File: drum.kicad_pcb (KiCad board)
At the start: 4 copper layers, 70 x 70 mm, 112 parts, among them J1001 NE8FAH, J101 CORTEX-DEBUG, J102 JAE_DX07S016JA3, J501 WAGO-2065, J502 WAGO-2065, J601 WAGO-2065, J602 WAGO-2065, J701 Conn_01x01, J702 Conn_01x01, J703 Conn_01x01, J704 Conn_01x01, J801 WAGO-2065, J802 WAGO-2065, J803 WAGO-2065, J901 NE8FAH, Q201 BSC010N04LS, Q202 BSC010N04LS, Q501 BSC010N04LS, Q601 BSC010N04LS, SW101 SW_Push, SW102 SW_Push, U1001 THVD24x2, U101 ATSAMD51J, U102 TPS78433QWDRBRQ1, U201 LM74502-Q1, U301 TPSM33625, U401 BTT6010, U701 TMC2130-LA, U801 74AHC1G125, U901 THVD24x2, Y101 32k768

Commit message: Update
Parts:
- moved INFO101 2.55 mm to (121.0, 117.5)
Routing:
- net GND: vias 100 -> 110
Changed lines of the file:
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@@
 	(footprint "V2_Production:Layer_Numbers"
 		(layer "F.Cu")
-		(at 121.5 115 -90)
+		(at 121 117.5 -90)
 		(property "Reference" "INFO101"
 			(at 0 -2.25 270)
@@
 			(polygon
 				(pts
-					(xy 120.9 116.6) (xy 120.9 113.4) (xy 122.1 113.4) (xy 122.1 116.6)
+					(xy 120.4 119.1) (xy 120.4 115.9) (xy 121.6 115.9) (xy 121.6 119.1)
 				)
 			)
@@
 	)
 	(via
+		(at 121 135)
+		(size 0.45)
+		(drill 0.2)
+		(layers "F.Cu" "B.Cu")
+		(remove_unused_layers yes)
+		(keep_end_layers yes)
+		(free yes)
+		(zone_layer_connections "In1.Cu" "In2.Cu")
+		(net 1)
+	)
+	(via
 		(at 160.75 92.25)
 		(size 0.45)
@@
 	)
 	(via
+		(at 121 115)
+		(size 0.45)
+		(drill 0.2)
+		(layers "F.Cu" "B.Cu")
+		(remove_unused_layers yes)
+		(keep_end_layers yes)
+		(free yes)
+		(zone_layer_connections "In1.Cu" "In2.Cu")
+		(net 1)
+	)
+	(via
+		(at 121 120)
+		(size 0.45)
+		(drill 0.2)
+		(layers "F.Cu" "B.Cu")
+		(remove_unused_layers yes)
+		(keep_end_layers yes)
+		(free yes)
+		(zone_layer_connections "In1.Cu" "In2.Cu")
+		(net 1)
+	)
+	(via
 		(at 154.5 108.75)
 		(size 0.45)
@@
 	)
 	(via
+		(at 189 80)
+		(size 0.45)
+		(drill 0.2)
+		(layers "F.Cu" "B.Cu")
+		(remove_unused_layers yes)
+		(keep_end_layers yes)
+		(free yes)
+		(zone_layer_connections "In1.Cu")
+		(net 1)
+	)
+	(via
+		(at 185 71)
+		(size 0.45)
+		(drill 0.2)
+		(layers "F.Cu" "B.Cu")
+		(remove_unused_layers yes)
+		(keep_end_layers yes)
+		(free yes)
+		(zone_layer_connections "In1.Cu")
+		(net 1)
+	)
+	(via
 		(at 160.5 83.5)
 		(size 0.45)
@@
 	)
 	(via
+		(at 145 71)
+		(size 0.45)
+		(drill 0.2)
+		(layers "F.Cu" "B.Cu")
+		(remove_unused_layers yes)
+		(keep_end_layers yes)
+		(free yes)
+		(zone_layer_connections "In1.Cu" "In2.Cu")
+		(net 1)
+	)
+	(via
 		(at 185.75 115.75)
 		(size 0.45)
@@
 	)
 	(via
+		(at 189 75)
+		(size 0.45)
+		(drill 0.2)
+		(layers "F.Cu" "B.Cu")
+		(remove_unused_layers yes)
+		(keep_end_layers yes)
+		(free yes)
+		(zone_layer_connections "In1.Cu")
+		(net 1)
+	)
+	(via
 		(at 166.5 101)
 		(size 0.45)
@@
 	)
 	(via
+		(at 121 125)
+		(size 0.45)
+		(drill 0.2)
+		(layers "F.Cu" "B.Cu")
+		(remove_unused_layers yes)
+		(keep_end_layers yes)
+		(free yes)
+		(zone_layer_connections "In1.Cu" "In2.Cu")
+		(net 1)
+	)
+	(via
 		(at 141.25 92.25)
 		(size 0.45)
@@
 	)
 	(via
+		(at 165 71)
+		(size 0.45)
+		(drill 0.2)
+		(layers "F.Cu" "B.Cu")
+		(remove_unused_layers yes)
+		(keep_end_layers yes)
+		(free yes)
+		(zone_layer_connections "In1.Cu")
+		(net 1)
+	)
+	(via
 		(at 157 104.75)
 		(size 0.45)
@@
 		(size 0.45)
 		(drill 0.2)
+		(layers "F.Cu" "B.Cu")
+		(remove_unused_layers yes)
+		(keep_end_layers yes)
+		(free yes)
+		(zone_layer_connections "In1.Cu" "In2.Cu")
+		(net 1)
+	)
+	(via
+		(at 121 130)
+		(size 0.45)
+		(drill 0.2)

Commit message: Update parts
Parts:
- C1001, C101, C102, C103, C104, C105, C106, C107, C108, C201, C202, C302, C305, C401, C402, C403, C404, C501, C601, C701, C706, C708, C709, C901: footprint Capacitor_SMD:C_0603_1608Metric -> V2_Capacitor_SMD:C_0603
- C109, C110: footprint Capacitor_SMD:C_0805_2012Metric -> V2_Capacitor_SMD:C_0805
- C301, C303, C304, C704, C705: footprint Capacitor_SMD:C_1210_3225Metric -> V2_Capacitor_SMD:C_1210
- C702, C703: footprint Capacitor_SMD:CP_Elec_6.3x5.8 -> V2_Capacitor_SMD:CP_Elec_6.3x7.7
- C707: value 0u470 -> 0u47; footprint Capacitor_SMD:C_0603_1608Metric -> V2_Capacitor_SMD:C_0603
- D101: footprint LED_SMD:LED_0603_1608Metric -> V2_LED:LED_0603
- D401: footprint Diode_SMD:D_SOD-523 -> V2_Diode_SMD:D_SOD-523
- D501, D601: footprint Diode_SMD:D_SOD-123F -> V2_Diode_SMD:D_SOD-123F
- FID101, FID102, FID103: value Fiducial -> Fiducial_Paste
- INFO102: value ORDER-NUMBER -> Order_Number
- J1001, J901: value NE8FAH -> NE8FAV
- J101: value CORTEX-DEBUG -> Cortex_Debug
- J102: value JAE_DX07S016JA3 -> DX07S016JA3
- J501, J502, J601, J602, J801, J802, J803: value WAGO-2065 -> WAGO 2065-100
- J701, J702, J703, J704: value Conn_01x01 -> WAGO 2065-100
- R1001, R101, R102, R103, R104, R201, R202, R301, R302, R401, R402, R403, R404, R405, R406, R407, R408, R409, R410, R701, R901: footprint Resistor_SMD:R_0603_1608Metric -> V2_Resistor_SMD:R_0603
- R702, R703: footprint Resistor_SMD:R_0805_2012Metric -> V2_Resistor_SMD:R_0805
- SW101, SW102: value SW_Push -> SKSG
- TVS101: value SMAJ36CA -> SMBJ36CA; footprint Diode_SMD:D_SMA -> V2_Diode_SMD:D_SMB
- U1001, U901: value THVD24x2 -> THVD2442
- U801: footprint Package_TO_SOT_SMD:SOT-23-5 -> V2_Package_TO_SOT_SMD:SOT-23-5
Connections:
- net USB-Shield renamed Shield

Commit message: Update library
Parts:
- TVS101: value SMBJ36CA -> SMBJ33CA
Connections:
- net +24V renamed +28V
- net /+24V-Supply renamed +VLINK
- net VBUS renamed +VBUS

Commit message: Update library
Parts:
- J101: value Cortex_Debug -> Cortex; footprint V2_Cortex_Debug:Cortex_Debug_Pad -> V2_Connector_Debug:Cortex
- U301: footprint V2_Converter_DCDC:TPSM33625 -> V2_Converter_DCDC:QFN-11
- U701: footprint V2_Driver_Stepper:QFN36-5X6 -> V2_Package_DFN_QFN:QFN36-5X6
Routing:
- net /SWCLK: track 11.3 -> 13.3 mm
- net GND: vias 110 -> 108
- net +3V3: vias 16 -> 15

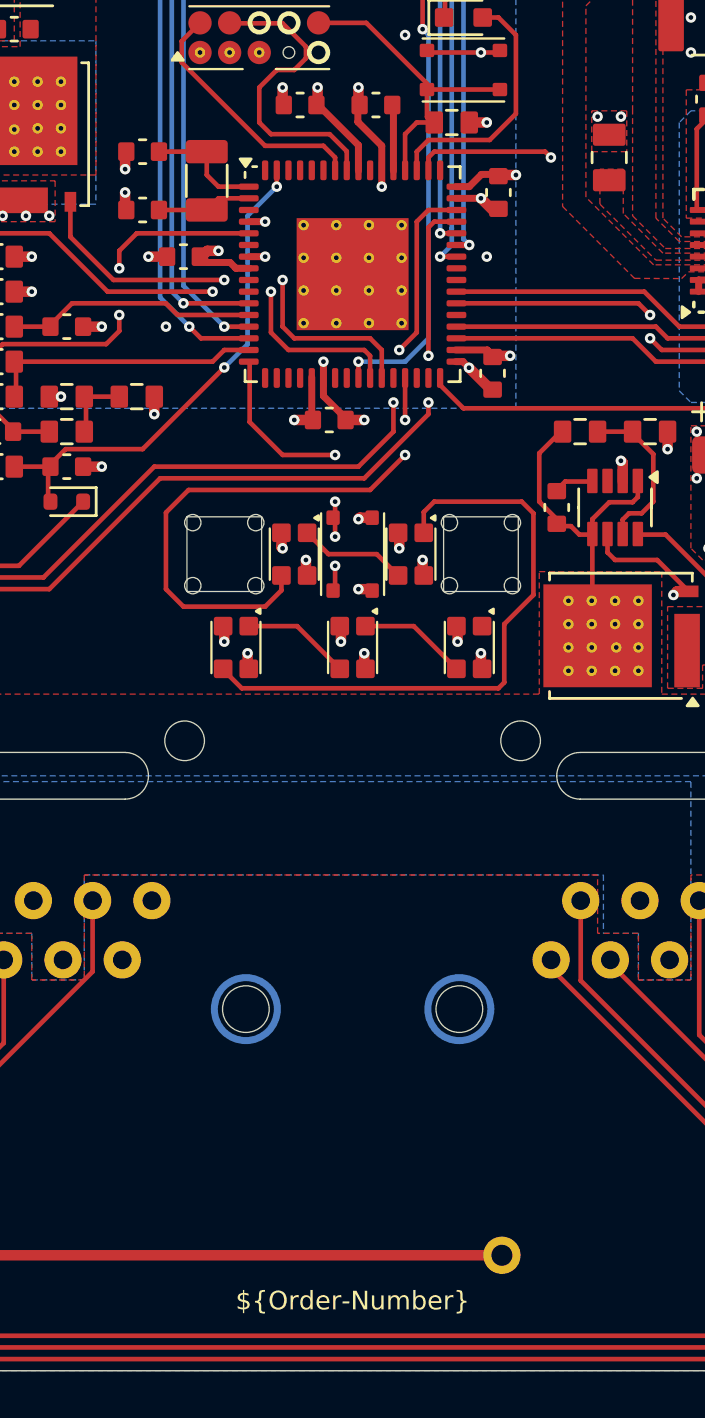
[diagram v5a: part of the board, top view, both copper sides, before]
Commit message: Replace Order_Number
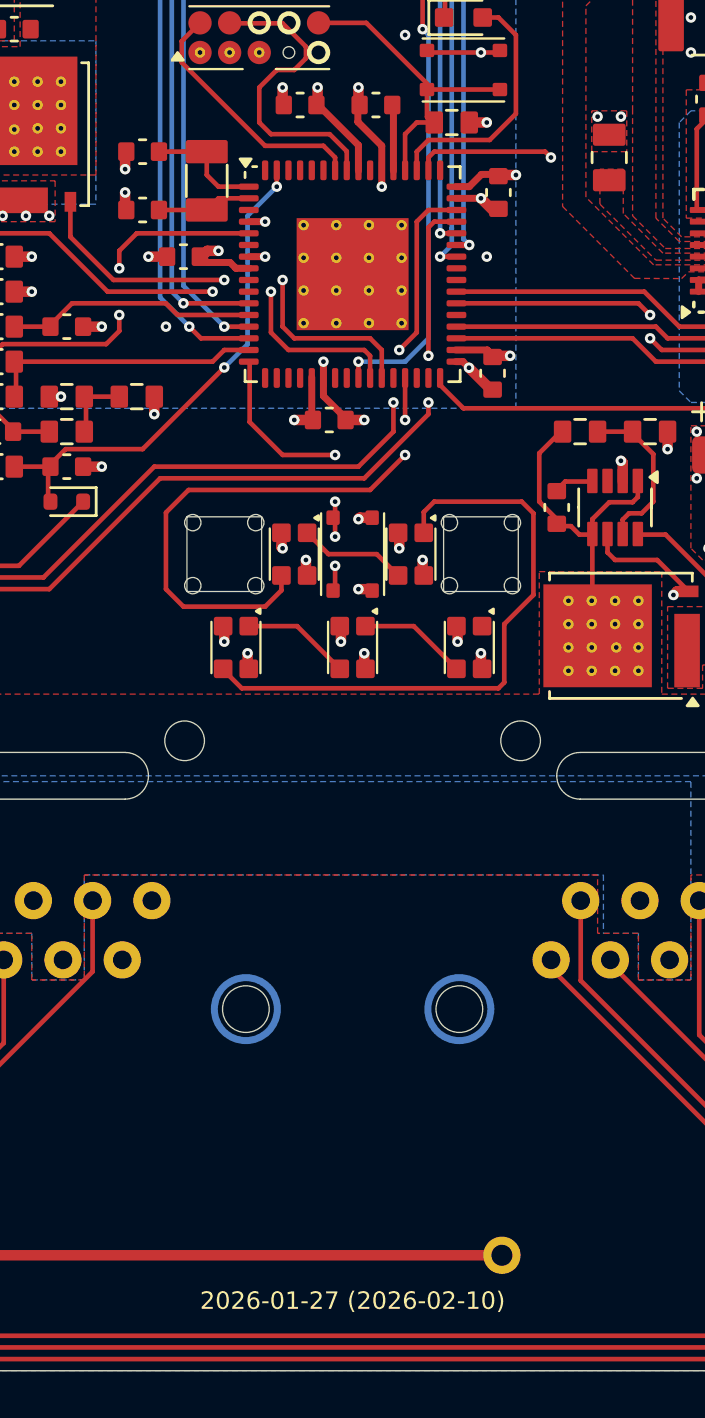
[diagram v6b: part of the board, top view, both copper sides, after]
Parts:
- H101, H102, H103, H104: value MountingHole_3mm -> 3mm
- INFO102: value Order_Number -> ~; footprint V2_Production:Order_Number -> V2_Production:Revision

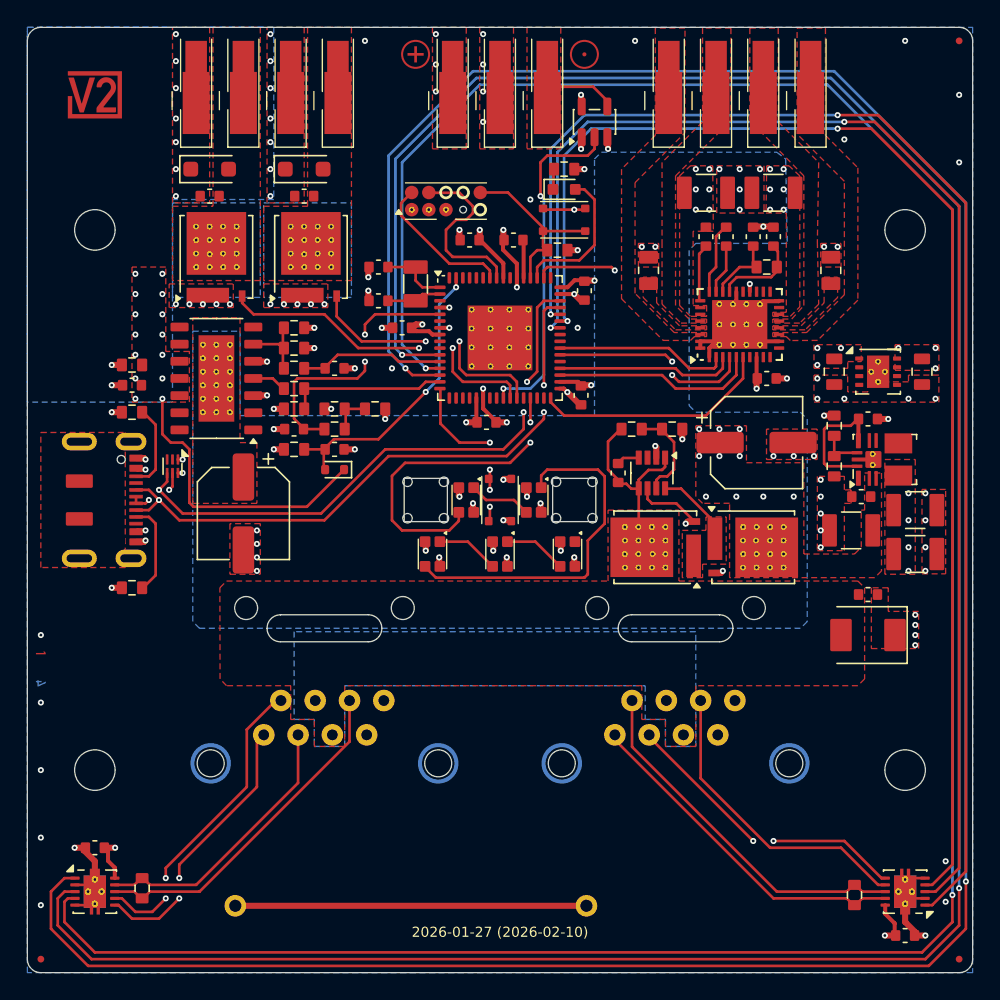
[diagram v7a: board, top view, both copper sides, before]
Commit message: Replace diode
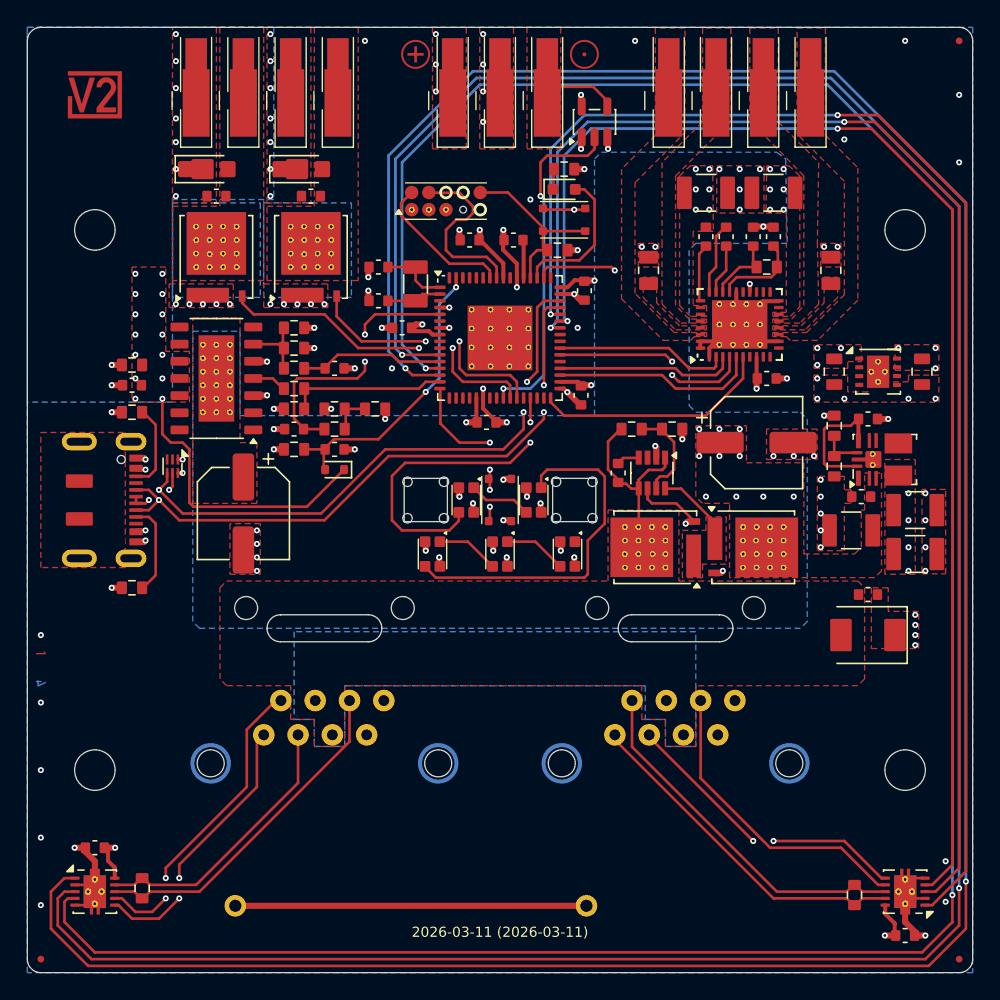
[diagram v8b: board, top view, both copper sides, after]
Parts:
- D501, D601: value S310FA -> PMEG6030AEXEX; footprint V2_Diode_SMD:D_SOD-123F -> V2_Diode_SMD:D_SOD-123HP
- U701: footprint V2_Package_DFN_QFN:QFN36-5X6 -> V2_Package_DFN_QFN:QFN-36-5X6
- moved C501 0.50 mm to (134.0, 82.5)
- moved C601 0.50 mm to (141.0, 82.5)
- moved D501 0.25 mm to (133.2, 80.5)
- moved D601 0.25 mm to (140.2, 80.5)
